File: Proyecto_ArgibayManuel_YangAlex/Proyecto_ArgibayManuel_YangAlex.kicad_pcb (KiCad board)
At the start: 2 copper layers, 159 x 89.5 mm, 61 parts, among them IC1 LM1117, J1 Conn_01x02, J2 Conn_01x01, J3 Con_1x2, J4 Con_1x3, J5 Conn_01x03_Pin, J6 Conn_01x07, J7 Con_ICSP, K1 RT314012, K2 RT314012, Q1 2N2222, Q2 2N2222, SW1 SW_Push, SW2 SW_Push, SW3 SW_Push, SW4 SW_Push, U1 PIC18F258-I_SO, U2 HDC2010YPAR, U3 LT1716IS5TRMPBF, U4 LT1716IS5TRMPBF, U5 TXS0108EPW, U6 DRV8871DDA, U7 DRV8871DDA, U8 MCP2551-I-P, X1 DB9, X2 DB9, Y1 Crystal

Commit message: Agrego cambios
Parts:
- removed R10: 0, Resistor_THT:R_Axial_DIN0204_L3.6mm_D1.6mm_P5.08mm_Vertical
- moved J1 104.0 mm to (204.0, 41.0), turned to 90 degrees
- moved J7 55.1 mm to (131.9, 55.5)
- moved REF** 28.0 mm to (230.5, 89.0)
- moved J6 22.5 mm to (226.0, 74.5)
- moved U6 20.5 mm to (203.5, 88.5)
- moved U7 20.5 mm to (203.5, 80.8)
- moved Ref 20.5 mm to (102.5, 89.5)
- moved REF** 19.8 mm to (230.5, 37.0)
- moved K2 19.4 mm to (210.2, 58.9), turned to 90 degrees
- moved K1 15.5 mm to (196.2, 58.5), turned to -90 degrees
- moved X1 14.9 mm to (163.0, 91.5), turned to 180 degrees
- moved X2 14.9 mm to (130.8, 91.5), turned to 180 degrees
- moved Q1 13.2 mm to (176.0, 67.0)
- moved D1 13.2 mm to (177.3, 72.8)
- moved Q2 12.7 mm to (176.0, 79.0)
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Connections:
- net CANH renamed CAN+
- net CANL renamed CAN-
- J1 pad 1: GND -> GNDPWR
- J6 pad 5: Calefactor -> Bomba
- J6 pad 6: Bomba -> Calefactor
- J6 pad 7: GND -> GNDPWR
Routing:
- net PGD: track 58.1 -> 5.06 mm
- net PGC: track 55.4 -> 8.49 mm
- net Calefactor: track 43.7 -> 13.6 mm
- net CAN-: track 45.3 -> 21.7 mm
- net VPP: track 57.7 -> 34.2 mm
- net CAN+: track 48.4 -> 25.8 mm
- net Net-(D2-K): track 21.3 -> 42.6 mm
- net Net-(D1-K): track 21.7 -> 41.0 mm
- net Motor_derecho_2: track 45.3 -> 31.3 mm
- net Motor_derecho_1: track 47.8 -> 34.1 mm
- net Motor_Izquierdo_1: track 43.6 -> 30.5 mm
- net Motor_izquierdo_2: track 40.6 -> 27.7 mm
- net RC6: track 34.6 -> 22.8 mm, vias 0 -> 2
- net C_R_Bombas_agua: track 44.3 -> 33.4 mm
- net RC7: track 35.8 -> 25.0 mm
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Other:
- board size 159 x 89.5 mm -> 139.5 x 64.5 mm

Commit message: Arreglo layout y esqumatico con las correcciones pasadas
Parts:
- added R14: 1k, Resistor_SMD:R_0805_2012Metric, F.Cu at (196.5, 41.0)
- added R15: 1k, Resistor_SMD:R_0805_2012Metric, F.Cu at (187.5, 85.4)
- C1, C10, C11, C12, C2, C3, C6, C7, C8, C9: footprint Capacitor_THT:CP_Radial_D5.0mm_P2.00mm -> Capacitor_SMD:C_0805_2012Metric
- moved J2 9.06 mm to (100.0, 72.5)
- moved D1 5.24 mm to (182.5, 72.5), turned to 180 degrees
- moved D2 4.24 mm to (183.0, 86.0), turned to 180 degrees
- moved J6 3.50 mm to (222.5, 74.5)
- moved K1 3.50 mm to (192.8, 58.5)
- moved K2 3.50 mm to (206.8, 58.9)
- moved U6 3.50 mm to (200.0, 88.5)
- moved U7 3.50 mm to (200.0, 80.8)
- moved J1 2.27 mm to (202.0, 40.0)
- moved C1 1.05 mm to (120.0, 41.5)
- moved C10 1.05 mm to (155.5, 48.5)
- moved C2 1.01 mm to (106.5, 78.3)
- moved C8 1.01 mm to (141.5, 48.5)
- moved C9 1.01 mm to (135.0, 48.5)
- moved C12 0.99 mm to (175.3, 46.0)
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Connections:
- D1 pad 1: Net-(D1-K) -> VBat
- D1 pad 2: GNDPWR -> Net-(D1-A)
- D2 pad 1: Net-(D2-K) -> VBat
- D2 pad 2: GNDPWR -> Net-(D2-A)
- K1 pad A2: Net-(D1-K) -> Net-(D1-A)
- K2 pad A2: Net-(D2-K) -> Net-(D2-A)
- Q1 pad 3: Net-(D1-K) -> Net-(D1-A)
- Q2 pad 3: Net-(D2-K) -> Net-(D2-A)
- R8 pad 1: C_R_Bombas_agua -> Net-(Q1-Pad2)
- R8 pad 2: Net-(Q1-Pad2) -> C_R_Bombas_agua
- R9 pad 1: C_R_Calefactor -> Net-(Q2-Pad2)
- R9 pad 2: Net-(Q2-Pad2) -> C_R_Calefactor
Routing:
- net Net-(D1-A): track 0.00 -> 48.2 mm
- net Net-(D2-A): track 0.00 -> 46.0 mm
- net Net-(D2-K): track 42.6 -> 0.00 mm
- net Net-(D1-K): track 41.0 -> 0.00 mm
- net GND: track 32.8 -> 52.9 mm, vias 21 -> 35
- net GNDPWR: track 35.8 -> 47.8 mm, vias 9 -> 16
- net +3.3V: track 33.0 -> 29.8 mm
- net C_R_Bombas_agua: track 33.4 -> 35.1 mm
- net PH_M_in2: track 12.9 -> 12.2 mm
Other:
- board size 139.5 x 64.5 mm -> 140 x 65 mm

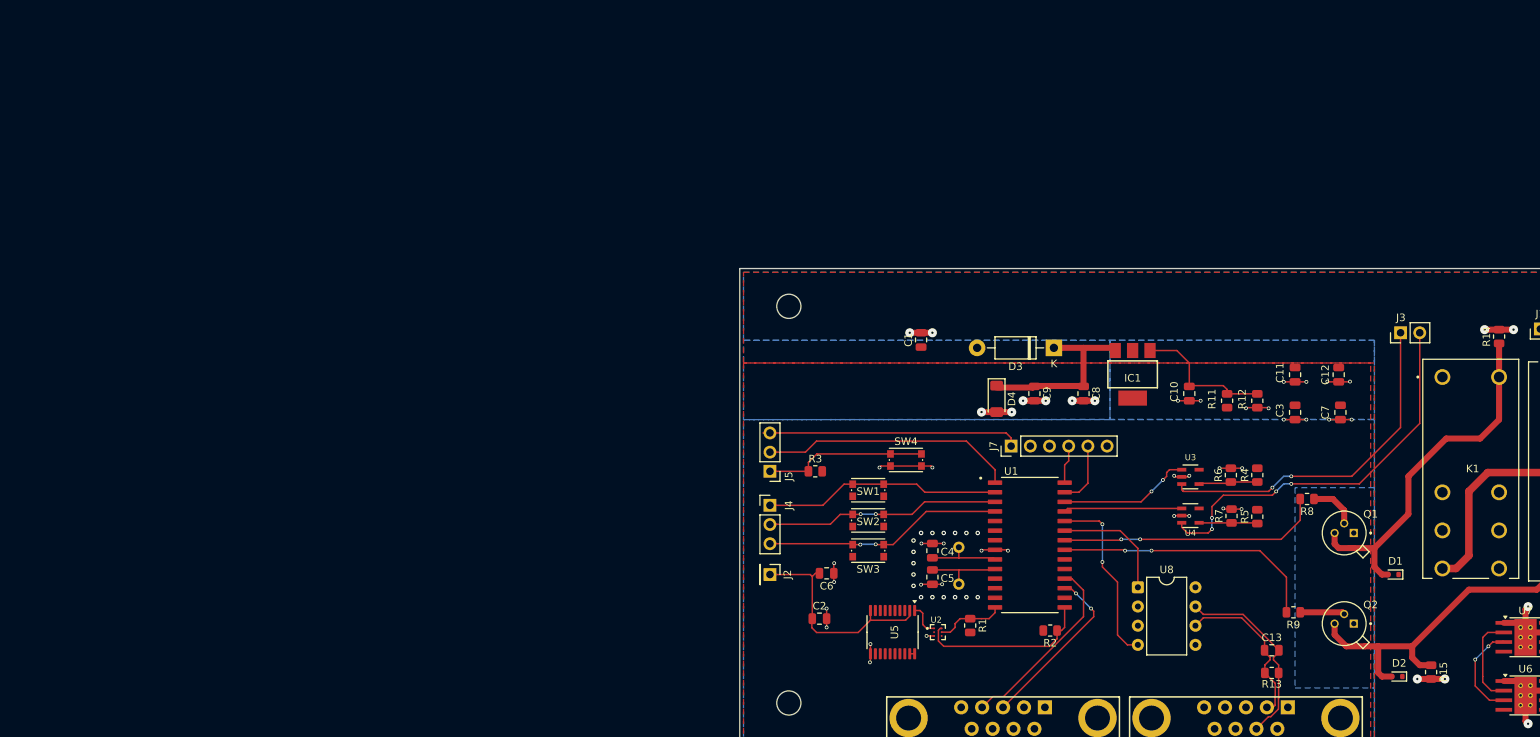
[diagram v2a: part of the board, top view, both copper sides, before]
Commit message: cambiar esquematico
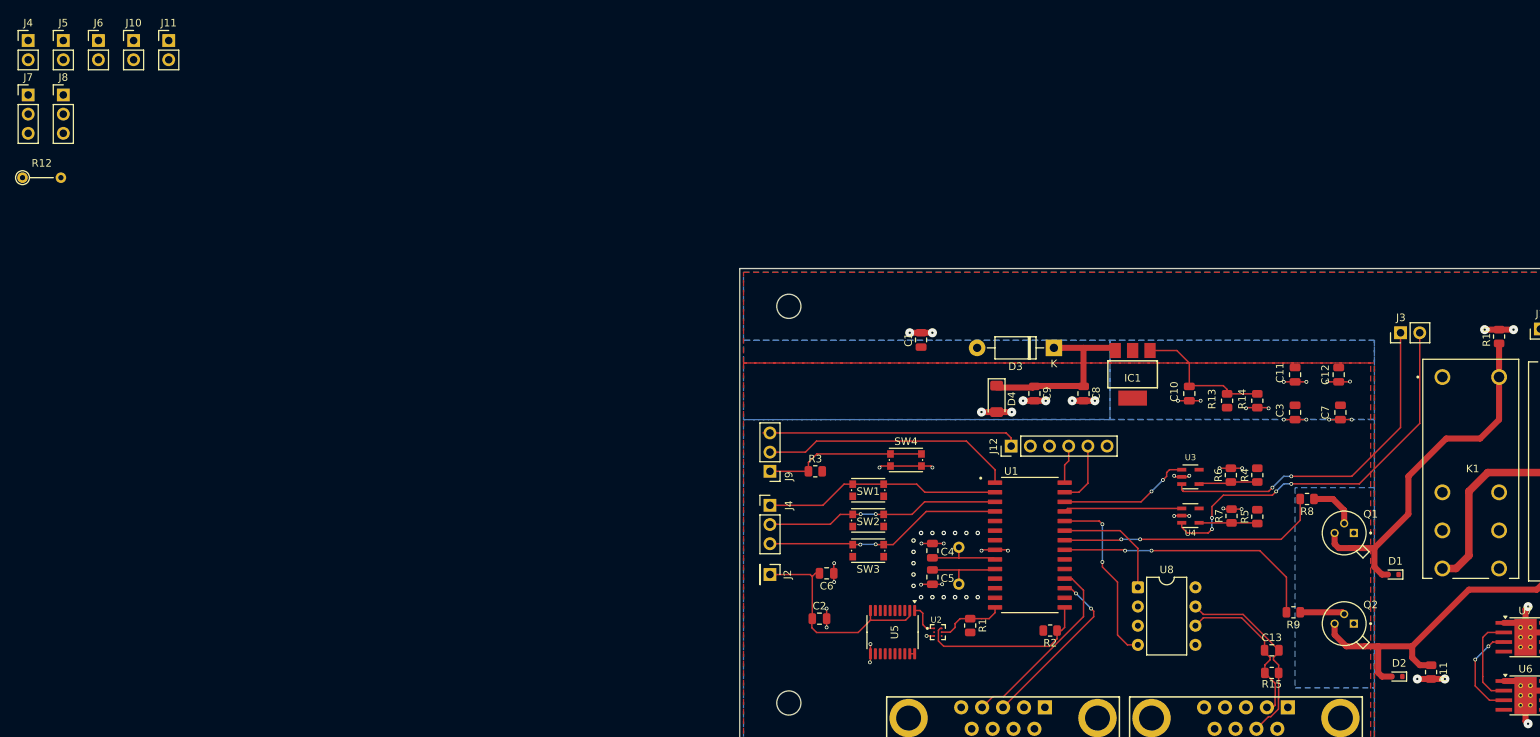
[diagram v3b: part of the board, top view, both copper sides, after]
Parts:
- added J10: Con_1x2, Connector_PinHeader_2.54mm:PinHeader_1x02_P2.54mm_Vertical, F.Cu at (15.8, 1.82)
- added J11: Con_1x2, Connector_PinHeader_2.54mm:PinHeader_1x02_P2.54mm_Vertical, F.Cu at (20.4, 1.82)
- added J4: Con_1x2, Connector_PinHeader_2.54mm:PinHeader_1x02_P2.54mm_Vertical, F.Cu at (1.82, 1.82)
- added J5: Con_1x2, Connector_PinHeader_2.54mm:PinHeader_1x02_P2.54mm_Vertical, F.Cu at (6.47, 1.82)
- added J6: Con_1x2, Connector_PinHeader_2.54mm:PinHeader_1x02_P2.54mm_Vertical, F.Cu at (11.1, 1.82)
- added J7: Conn_01x03, Connector_PinHeader_2.54mm:PinHeader_1x03_P2.54mm_Vertical, F.Cu at (1.82, 9.03)
- added J8: Conn_01x03, Connector_PinHeader_2.54mm:PinHeader_1x03_P2.54mm_Vertical, F.Cu at (6.47, 9.03)
- added R12: 0, Resistor_THT:R_Axial_DIN0204_L3.6mm_D1.6mm_P5.08mm_Vertical, F.Cu at (1.07, 20.0)
- C4, C5: value 40pF -> 33pF
- renumbered J7 to J12, J5 to J9, R14 to R10, R15 to R11, R11 to R13, R12 to R14, R13 to R15

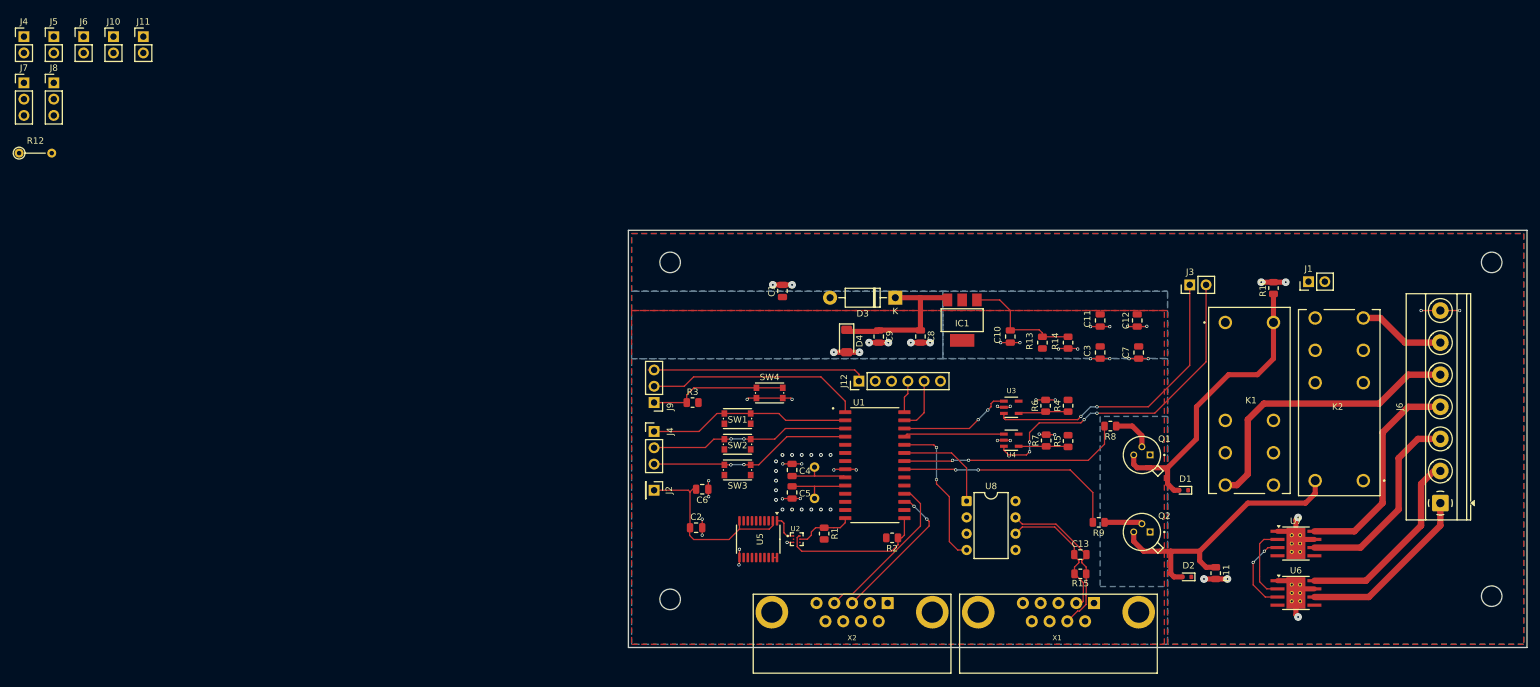
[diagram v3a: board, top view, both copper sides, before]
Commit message: Cambio de la PCB(por el cambio de elos conectores)
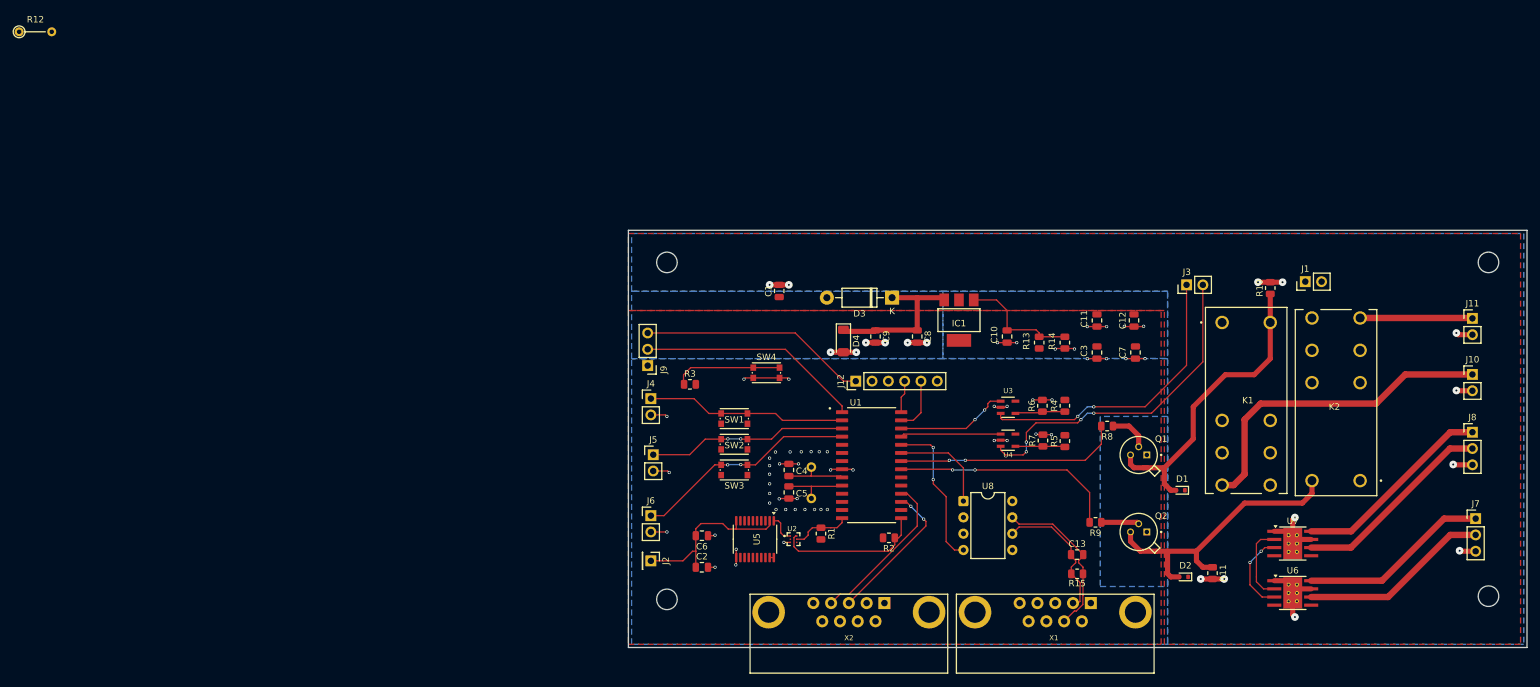
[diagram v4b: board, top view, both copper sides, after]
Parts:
- removed the J4 at (100.0, 63.3)
- removed the J6 at (222.5, 74.5)
- moved J7 236.1 mm to (228.0, 76.9)
- moved J8 227.6 mm to (227.5, 63.5)
- moved J10 218.2 mm to (227.5, 54.5)
- moved J11 211.7 mm to (227.5, 45.7)
- moved J6 115.7 mm to (99.5, 76.5)
- moved J5 113.9 mm to (99.9, 67.0)
- moved J4 112.8 mm to (99.5, 58.2)
- moved R12 18.9 mm to (1.07, 1.07)
- moved J2 11.0 mm to (99.5, 83.5)
- moved C6 7.24 mm to (107.5, 79.6)
- moved C2 6.23 mm to (107.5, 84.5)
- moved J9 5.85 mm to (99.0, 53.1)
- moved SW4 3.18 mm to (117.5, 54.2)
- moved R3 2.87 mm to (105.6, 56.0)
- moved C1 0.50 mm to (119.5, 41.5)
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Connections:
- J7 pad 1: Motor_izquierdo_2 -> Motor_Izquierdo_1
- J7 pad 2: Motor_Izquierdo_1 -> Motor_izquierdo_2
- J8 pad 1: Motor_derecho_2 -> Motor_derecho_1
- J8 pad 2: Motor_derecho_1 -> Motor_derecho_2
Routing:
- net Bomba: track 45.6 -> 51.1 mm
- net GND: track 52.9 -> 57.8 mm, vias 35 -> 55
- net GNDPWR: track 47.8 -> 52.2 mm, vias 16 -> 18
- net Net-(J9-Pin_1): track 21.7 -> 17.5 mm
- net Calefactor: track 13.6 -> 17.5 mm
- net Int_Bomba_de_Agua: track 31.7 -> 35.1 mm
- net Motor_derecho_1: track 34.1 -> 31.5 mm
- net Motor_izquierdo_2: track 27.7 -> 29.6 mm
- net +3.3V: track 29.8 -> 28.1 mm
- net VPP: track 34.2 -> 35.5 mm
- net MCLR: track 33.7 -> 34.9 mm
- net Motor_Izquierdo_1: track 30.5 -> 29.6 mm
- net VCC: vias 17 -> 0

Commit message: layout
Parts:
- removed R12: 0, Resistor_THT:R_Axial_DIN0204_L3.6mm_D1.6mm_P5.08mm_Vertical
- removed the REF** at (230.0, 89.0)
- removed the REF** at (230.0, 37.0)
- removed Ref: MountingHole_3.2mm_M3, MountingHole:MountingHole_3.2mm_M3
- added REF**: MountingHole_3.2mm_M3, MountingHole:MountingHole_3.2mm_M3, F.Cu at (223.5, 90.5)
- added REF**: MountingHole_3.2mm_M3, MountingHole:MountingHole_3.2mm_M3, F.Cu at (102.0, 90.5)
- added REF**: MountingHole_3.2mm_M3, MountingHole:MountingHole_3.2mm_M3, F.Cu at (223.5, 37.0)
- moved X1 4.61 mm to (159.5, 88.0)
- moved J10 4.53 mm to (223.0, 54.0)
- moved J11 4.53 mm to (223.0, 45.2)
- moved J7 4.53 mm to (223.5, 76.4)
- moved J8 4.53 mm to (223.0, 63.0)
- moved X2 3.96 mm to (128.3, 88.1)
- moved C13 2.89 mm to (164.5, 80.0)
- moved R15 2.89 mm to (164.5, 83.0)
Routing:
- net GNDPWR: track 52.2 -> 42.0 mm, vias 18 -> 14
- net Net-(J9-Pin_1): track 17.5 -> 24.3 mm
- net GND: track 57.8 -> 52.6 mm, vias 55 -> 70
- net Motor_izquierdo_2: track 29.6 -> 25.3 mm
- net Motor_Izquierdo_1: track 29.6 -> 25.3 mm
- net Bomba: track 51.1 -> 46.8 mm
- net Calefactor: track 17.5 -> 13.3 mm
- net CAN-: track 21.7 -> 18.8 mm
- net CAN+: track 25.8 -> 23.6 mm
- net RC6: track 22.8 -> 24.9 mm
- net RC7: track 25.0 -> 27.0 mm
- net Motor_derecho_2: track 31.5 -> 29.6 mm
- net Motor_derecho_1: track 31.5 -> 30.2 mm
- net Int_Bomba_de_Agua: track 35.1 -> 35.7 mm
- added copper zone on F.Cu, net GND
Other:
- board size 140 x 65 mm -> 133 x 66 mm
